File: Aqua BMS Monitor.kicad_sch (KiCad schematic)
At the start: 92 parts, among them J1 Conn_01x05_Pin, J2 Conn_01x04, J3 Conn_01x02_Pin, J4 Conn_01x04, J5 Conn_01x04, Q1 NPN, Q2 NMOS, Q3 NMOS, Q4 PMOS, U1 BQ76952PFBR

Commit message: Initial setup and some organization
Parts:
- added C00, C1-0, C2-1, C3-2, C4-3: 220nF, symbol Device:C
- added Cellin1: 1 low 5 high, symbol Connector:Conn_01x05_Pin
- added MainBattIn: Main lines, symbol Connector:Conn_01x02_Pin
- added RC0, RC1, RC2, RC3, RC4: 20, symbol Device:R
- added TP12: TestPoint, symbol Connector:TestPoint
- Cellin: renamed from J1; value Conn_01x05_Pin -> 1 low 5 high
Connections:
- net 16P: no longer Cellin.5 (Pin_5), R1.1
- net VSS: now also C00.2, C1-0.2, MainBattIn.2 (Pin_2)
- net Cell3: now reaches U1.1 (VC15), U1.10 (VC6), U1.11 (VC5), U1.12 (VC4), U1.2 (VC14), U1.3 (VC13), U1.4 (VC12), U1.5 (VC11), U1.6 (VC10), U1.7 (VC9), U1.8 (VC8), U1.9 (VC7)
- net Cell3: now also U1.13 (VC3), C3-2.2, C4-3.1, RC3.2; no longer R1.2, U1.48 (VC16)
- net at C21.2, R2.2: no longer U1.13 (VC3)
- net at C1.2, C21.1, R3.2: no longer U1.14 (VC2)
- net at C1.1, C3.1, R4.2: no longer U1.15 (VC1)
- new net: Cellin1.4 (Pin_4), RC3.1
- new net: C4.1, Cellin.1 (Pin_1), TP5.1
- new net: Cellin1.2 (Pin_2), RC1.1
- new net: R8.2, R9.2, TP6.1
- new net: Cellin1.1 (Pin_1), RC0.1
- new net: Cellin1.3 (Pin_3), RC2.1
- new net: Cellin1.5 (Pin_5), RC4.1
- new net BAT+: MainBattIn.1 (Pin_1)
- new net Cell0: C00.1, RC0.2, TP12.1, U1.16 (VC0)
- new net Cell1: C1-0.1, C2-1.1, RC1.2, U1.15 (VC1)
- new net Cell2: C2-1.2, C3-2.1, RC2.2, U1.14 (VC2)
- new net Cell4: C4-3.2, RC4.2, U1.48 (VC16)
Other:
- note added: "Battery in"
- note added: "Cells"
- note added: "Grounding will be something to look at, cells are not necessarly attached to ground normally"
- note added: "Needs tie to ground, I think this right..."
- moved on the sheet: C1, C10, C15, C16, C2, C21, C28, C29, C3, C30, C31, C4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

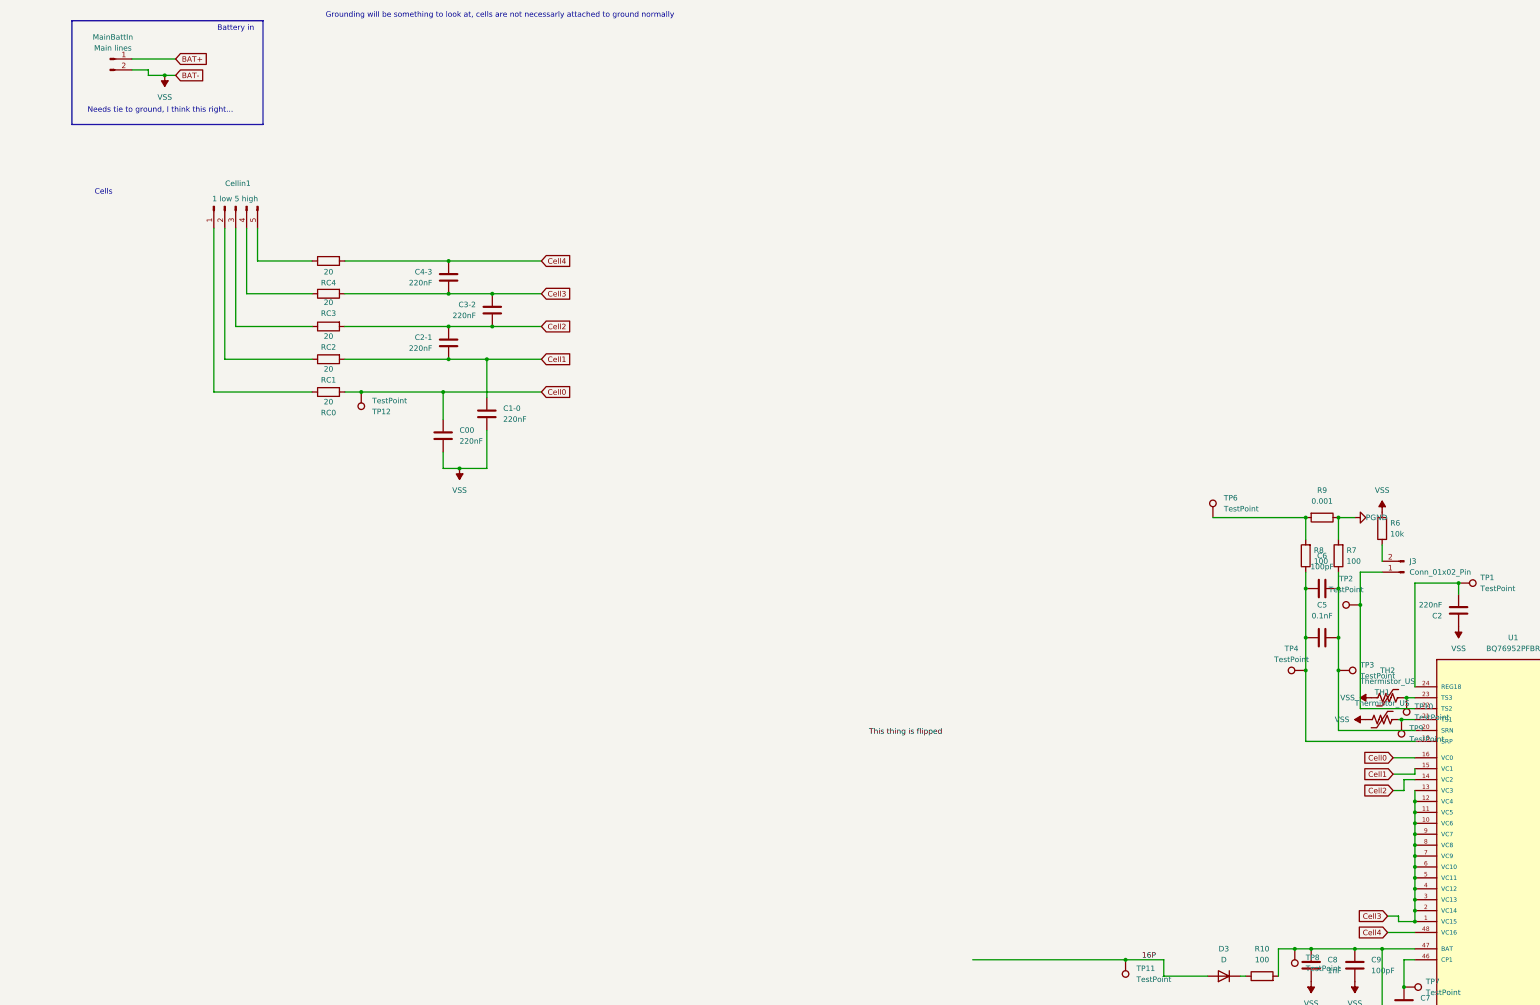
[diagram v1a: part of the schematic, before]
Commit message: Updates
Cell monitor and shunt resistor complete
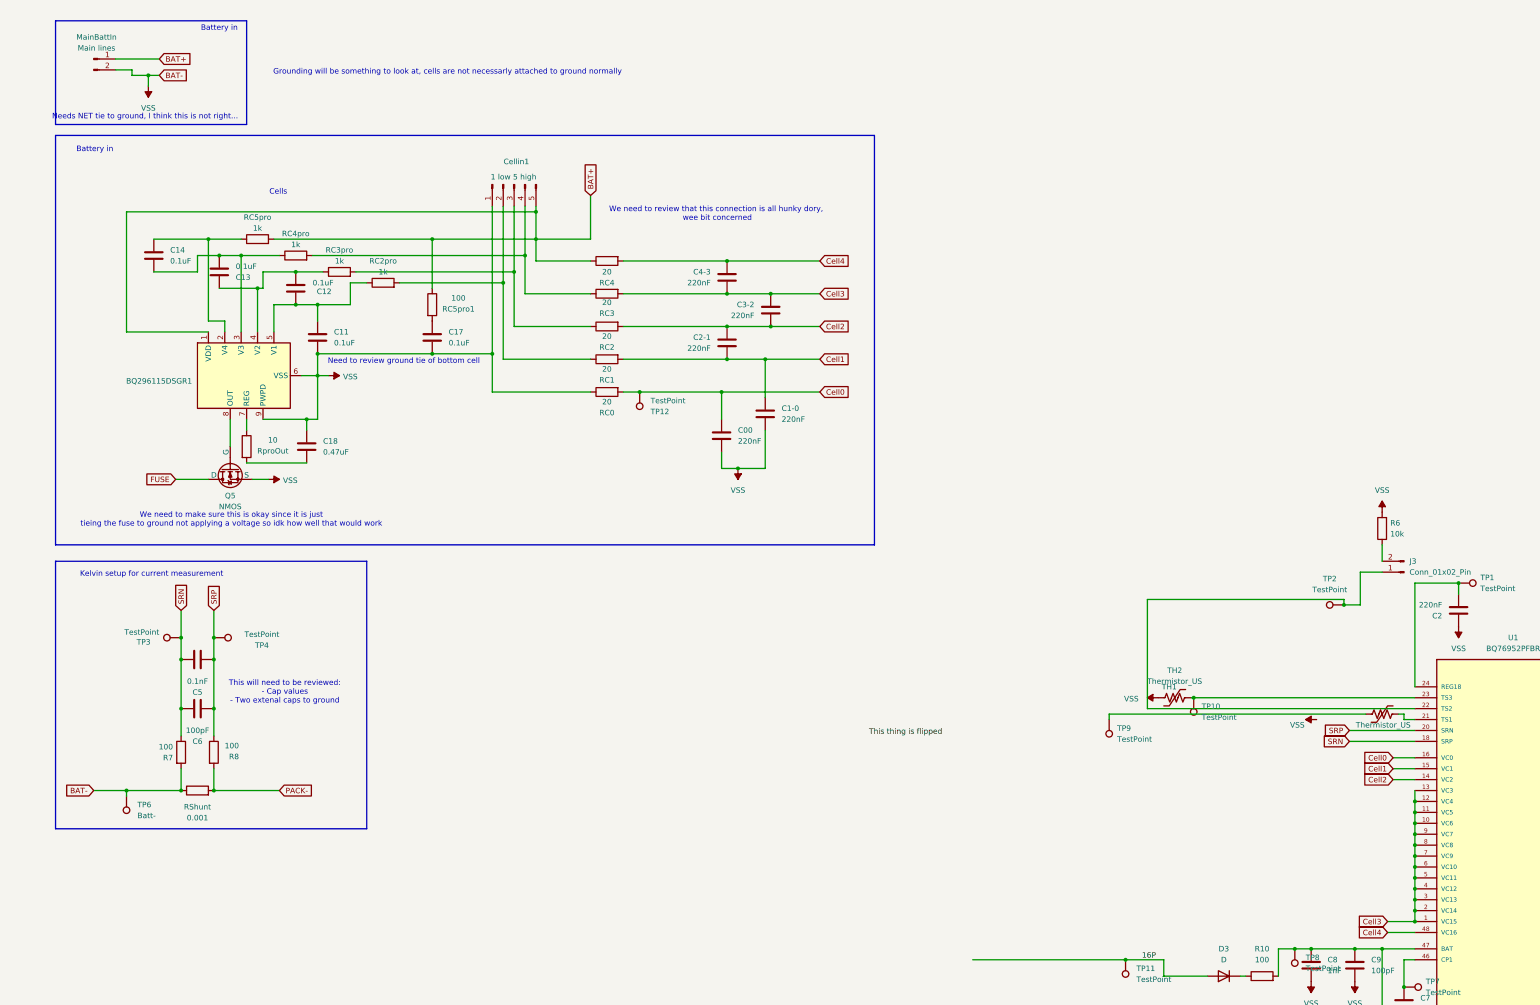
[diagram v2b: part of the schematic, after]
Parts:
- added BQ296115DSGR1: ~, symbol New_Library:BQ296115DSGR
- added C11, C12, C13, C14, C17: 0.1uF, symbol Device:C
- added C18: 0.47uF, symbol Device:C
- added Q5: NMOS, symbol Simulation_SPICE:NMOS
- added RC2pro, RC3pro, RC4pro, RC5pro: 1k, symbol Device:R
- added RC5pro1: 100, symbol Device:R
- added RproOut: 10, symbol Device:R
- TP6: value TestPoint -> Batt-
- renumbered R9 to RShunt
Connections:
- net BAT+: now also Cellin1.5 (Pin_5), RC4.1, BQ296115DSGR1.1 (VDD), RC5pro.2, RC5pro1.1
- net PGND: no longer R7.2, RShunt.1
- net VSS: now also Cellin1.1 (Pin_1), R7.2, RC0.1, RShunt.1, TP6.1, BQ296115DSGR1.6 (VSS), BQ296115DSGR1.9 (PWPD), C11.1, C17.2, C18.1, Q5.3 (S); no longer TH1.1
- net at Cellin1.4 (Pin_4), RC3.1: now also RC4pro.2
- net SRP: now reaches C5.2, C6.2, R8.1, TP4.1
- net SRP: now also U1.20 (SRN); no longer U1.18 (SRP)
- net SRN: now reaches C5.1, C6.1, R7.1, TP3.1
- net SRN: now also U1.18 (SRP); no longer U1.20 (SRN)
- net at TH1.2, U1.21 (TS1): no longer TP9.1
- net at Cellin1.2 (Pin_2), RC1.1: now also RC2pro.2
- net PACK-: now reaches R8.2, RShunt.2
- net PACK-: no longer TP6.1
- net at Cellin1.3 (Pin_3), RC2.1: now also RC3pro.2
- new net: BQ296115DSGR1.2 (V4), C14.1, RC5pro.1
- new net: BQ296115DSGR1.3 (V3), C13.2, C14.2, RC4pro.1
- new net: TH1.1, TP9.1
- new net: C17.1, RC5pro1.2
- new net: BQ296115DSGR1.5 (V1), C11.2, C12.1, RC2pro.1
- new net: BQ296115DSGR1.4 (V2), C12.2, C13.1, RC3pro.1
- new net: BQ296115DSGR1.8 (OUT), Q5.2 (G)
- new net: BQ296115DSGR1.7 (REG), RproOut.1
- new net: C18.2, RproOut.2
- new net FUSE: Q5.1 (D)
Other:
- note added: "Kelvin setup for current measurement"
- note added: "Need to review ground tie of bottom cell"
- note added: "Needs NET tie to ground, I think this is not right..."
- note added: "This will need to be reviewed: - Cap values - Two extenal caps to ground"
- note added: "We need to make sure this is okay since it is just tieing the fuse to ground not applying a voltage so idk how well that would work"
- note added: "We need to review that this connection is all hunky dory, wee bit concerned"
- note removed: "Needs tie to ground, I think this right..."
- moved on the sheet: C00, C1-0, C2-1, C3-2, C4-3, C5, C6, Cellin1, MainBattIn, R7, R8, RC0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

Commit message: Updates
Thermosister and BAT/CP1 circuit updated
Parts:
- removed C21: 220nF, symbol Device:C
- removed C7: 0.47nF, symbol Device:C
- removed C8: 1nF, symbol Device:C
- removed C9: 100pF, symbol Device:C
- removed Cellin: 1 low 5 high, symbol Connector:Conn_01x05_Pin
- removed D3: D, symbol Device:D
- removed J3: Conn_01x02_Pin, symbol Connector:Conn_01x02_Pin
- removed R10: 100, symbol Device:R
- removed R2, R3, R4: 20, symbol Device:R
- removed R6: 10k, symbol Device:R
- removed TH1, TH2: Thermistor_US, symbol Device:Thermistor_US
- removed TP10, TP11, TP7, TP8: TestPoint, symbol Connector:TestPoint
- added D3: 100V, symbol Device:D_Schottky
- added J1: Conn_01x02_Pin, symbol Connector:Conn_01x02_Pin
- added R9: 10k, symbol Device:R
- added TH3, TH4: Thermistor_US, symbol Device:Thermistor_US
- added TP13, TP14, TP15: TestPoint, symbol Connector:TestPoint
- C1: value 220nF -> 1nF
- C3: value 220nF -> 100pF
- C4: value 220nF -> 0.47nF
- R1: value 20 -> 100
- TP2: value TestPoint -> BAT+
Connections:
- net BAT+: now also TP2.1, D3.2 (A)
- net VSS: now also C1.2, R9.2, TH3.2, TH4.2; no longer C4.2
- net BAT: now reaches U1.47 (BAT)
- net BAT: now also C1.1, C3.1, C4.1, R1.2, TP5.1
- net TS1: now reaches U1.21 (TS1)
- net TS1: now also TH3.1, TP14.1
- net TS2: now reaches U1.22 (TS2)
- net TS2: now also J1.1 (Pin_1), TP15.1; no longer TP2.1
- net TS3: now reaches U1.23 (TS3)
- net TS3: now also TH4.1, TP13.1
- net CP1: now reaches U1.46 (CP1)
- net CP1: now also C4.2, TP9.1
- net at R1.1: now also D3.1 (K)
- new net: J1.2 (Pin_2), R9.1
- no-connect marks 0 -> 1
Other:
- note added: "- values will likely need to be better tailored to our application - CP will likely be used, but depends on main line circuit"
- note added: "Battery and Charge pump circuit"
- note added: "TS1, TS2, TS3 circuit"
- note added: "This guy is meant for wake ups this could likely become another themistor While it is two extenrnal connection pins we need to figure this out If this is the only way to wake the cell up we'll need this because getting slept would suck"
- moved on the sheet: C2, D1, D2, GD1, GD2, J2, R22, TP1

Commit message: Main circuits done
All circuits I (kinda) understand are organised
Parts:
- removed C16: 22nF, symbol Device:C
- removed C28, C29: 0.1uF, symbol Device:C
- removed D1, D2: D_TVS, symbol Device:D_TVS
- removed D4: D_Zener, symbol Device:D_Zener
- removed D5, D6, D7: 16V, symbol Device:D_Zener
- removed D7: 100V, symbol Device:D_Zener
- removed D8: 100V, symbol Device:D_Schottky
- removed GD1, GD2: GDT_2Pin, symbol Device:GDT_2Pin
- removed J2: Conn_01x04, symbol Connector_Generic:Conn_01x04
- removed Q1: NPN, symbol Simulation_SPICE:NPN
- removed Q2, Q3: NMOS, symbol Simulation_SPICE:NMOS
- removed Q4: PMOS, symbol Simulation_SPICE:PMOS
- removed R22: R 1.0k, symbol Device:R
- removed R31: R 10M, symbol BQ76952PFBR:R
- removed R32, R33: 10M, symbol BQ76952PFBR:R
- removed R34: 0, symbol BQ76952PFBR:R
- removed R35: 10k, symbol BQ76952PFBR:R
- removed R37, R39, R41, R42, R43, R44, R45: R 5.1k, symbol BQ76952PFBR:R
- removed R40: R 7.5k, symbol BQ76952PFBR:R
- removed TP16, TP17, TP19, TP22, TP23: TestPoint, symbol Connector:TestPoint
- added C7: 0.1uF, symbol Device:C
- added C8: 1uF, symbol Device:C
- added C9: 22nF, symbol Device:C
- added D1: 100V, symbol Device:D_Zener
- added D10, D12, D9: 16V, symbol Device:D_Zener
- added D11: 100V, symbol Device:D_Schottky
- added D2: D_Zener, symbol Device:D_Zener
- added Q1, Q7: NMOS, symbol Simulation_SPICE:NMOS
- added Q6: NPN, symbol Simulation_SPICE:NPN
- added Q8: PMOS, symbol Simulation_SPICE:PMOS
- added R10, R13, R14, R3, R4, R6: R 5.1k, symbol BQ76952PFBR:R
- added R12: R 10M, symbol BQ76952PFBR:R
- added R16: R 7.5k, symbol BQ76952PFBR:R
- added R17: 0, symbol BQ76952PFBR:R
- added R18, R19: 10M, symbol BQ76952PFBR:R
- added R2: 300, symbol BQ76952PFBR:R
- added R21: 10k, symbol BQ76952PFBR:R
- added TP10, TP11, TP18, TP7, TP8: TestPoint, symbol Connector:TestPoint
- C15: value 1uF -> 0.1uF
- R11: value 300 -> R 5.1k
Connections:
- net BAT+: now also C10.1, D9.2 (A), Q1.1 (D), R12.2
- net FUSE: now also U1.38 (FUSE)
- net PGND: now also D11.2 (A)
- net REG1: now also C8.2; no longer C15.2
- net VSS: now also C7.2, C8.1, C9.2; no longer C10.2, C15.1
- net CHG: now reaches U1.45 (CHG)
- net CHG: now also R11.1, TP10.1
- net at R11.2: now also D9.1 (K), Q1.2 (G), R12.1, TP18.1
- net REGIN: now reaches U1.36 (REGIN)
- net REGIN: now also C9.1, Q6.3 (E)
- net BREG: now reaches U1.37 (BREG)
- net BREG: now also Q6.2 (B)
- net LD: now reaches U1.41 (LD)
- net LD: now also R4.1, TP8.1
- net PACK: now reaches U1.42 (PACK)
- net PACK: now also R3.1, TP7.1; no longer TP21.1
- net DSG: now reaches U1.43 (DSG)
- net DSG: now also D2.1 (K), R14.1, TP11.1
- net PACK+: now reaches C30.1, E3.3, J5.1 (Pin_1), J5.2 (Pin_2)
- net PACK+: now also C15.2, TP21.1, D10.2 (A), D12.2 (A), Q7.3 (S), Q8.1 (D), R10.2, R18.2, R19.2, R6.2
- new net: D11.1 (K), R21.1
- new net: D12.1 (K), Q8.2 (G), R19.1, R21.2
- new net: R13.1, R14.2
- new net: D10.1 (K), Q8.3 (S), R13.2, R16.2, R17.1, R18.1
- new net: R10.1, R4.2
- new net: R3.2, R6.1
- new net: C10.2, C15.1
- new net: C7.1, Q6.1 (C), R2.1
- new net: Q7.2 (G), R17.2
- new net: D1.1 (K), R2.2
- new net: D2.2 (A), R16.1
- new net CD: D1.2 (A), Q1.3 (S), Q7.1 (D)
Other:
- note added: "Charge/Discharge circuit V1"
- note added: "I think these are not always tied to ground"
- note added: "Likely something we want in the big charge/discharge circuit"
- note added: "May be connect to something, may not!"
- note added: "May need to change resistor value and arrangement"
- note added: "May need to meddle with values otherwise fine"
- note added: "Pack and LD setup"
- note added: "Reg circuit"
- note added: "This will likely be changed but idk for now"
- note added: "Whoops I accidently disconnected this"
- note added: "You need to figure out what net this is"
- moved on the sheet: R15, TP20

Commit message: Commits before fork
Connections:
- net BAT+: now also Q1.3 (S); no longer Q1.1 (D)
- net CD: now also Q1.1 (D); no longer Q1.3 (S)
- net VSS: no longer U1.29 (CFETOFF), U1.30 (DFETOFF)
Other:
- note added: "I think these are not always tied to ground, we may have a use case"
- note added: "connection protection"
- note removed: "I think these are not always tied to ground"
- moved on the sheet: C2, D5, D6, GD3, GD4, J4, Q1, R15, R20, R23, R24, R5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

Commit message: Big Updates
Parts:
- removed J1: Conn_01x02_Pin, symbol Connector:Conn_01x02_Pin
- added C16: 1uF, symbol Device:C
- added C19, C20, C21, C22: 0.1uF, symbol Device:C
- added D4: 100V, symbol Device:D_Schottky
- added D7: 100V, symbol Device:D_Zener
- added MainBattIn1: Main lines, symbol Connector:Conn_01x02_Pin
- added Q2, Q3: PMOS, symbol Simulation_SPICE:PMOS
- added R22: 10M, symbol Device:R
- added R25, R30: R 10M, symbol BQ76952PFBR:R
- added R26, R28: 1k, symbol BQ76952PFBR:R
- added R27, R29: 5.1k, symbol BQ76952PFBR:R
- added SW1: Button, symbol Switch:SW_DPST_x2
- added TP16, TP22: TestPoint, symbol Connector:TestPoint
- C4: value 0.47nF -> 0.47uF
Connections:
- net BAT+: now also C19.1, C21.1, Q3.3 (S), R26.1, R30.1
- net BREG: now also R22.2
- net TS2: now also SW1.1 (A)
- net VSS: now also C16.1, MainBattIn1.2 (Pin_2), R22.1
- net at D5.2 (A2), D6.2 (A2), GD4.3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: no longer GD3.3, R24.2
- net at J4.3 (Pin_3), U1.26 (SCL), U1.44 (NC): now also GD3.3, R24.2
- net REG2: now reaches U1.34 (REG2)
- net REG2: now also C16.2
- net PDSG: now reaches U1.39 (PDSG)
- net PDSG: now also R29.1
- net PCHG: now reaches U1.40 (PCHG)
- net PCHG: now also R27.1
- net at D3.1 (K), R1.1: now also D4.1 (K)
- net at R9.1: now also SW1.2 (B)
- net at D1.1 (K), R2.2: now also D7.1 (K)
- net Cell0 renamed Cell1-
- net Cell1 renamed Cell1+/2-
- net Cell2 renamed Cell2+/3-
- net Cell3 renamed Cell3+/4-
- net Cell4 renamed Cell4+
- net REG1 renamed MCU
- new net: Q3.1 (D), R28.1
- new net: Q2.1 (D), R26.2
- new net: Q2.2 (G), R25.1, R27.2
- new net: Q3.2 (G), R29.2, R30.2
- new net: C21.2, C22.1
- new net: C19.2, C20.1
- new net CPACK+: C20.2, Q2.3 (S), R25.2, TP22.1
- new net DPACK+: C22.2, R28.2, TP16.1
- new net PWR+: D4.2 (A), D7.2 (A), MainBattIn1.1 (Pin_1)
- no-connect marks 1 -> 2
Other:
- note added: "- values will likely need to be better tailored to our application - CP is the power for CHG or DSG - There is an in depth discussion on how to select these in the application report"
- note added: "44 should also be NC -> not present on this"
- note added: "Can be split for heat disipation - Vid 440"
- note added: "DDSG SCHG used for comunicating the status of the fet"
- note added: "External 12V supply in"
- note added: "Gate resistors used to keep turn off and transients from being too high"
- note added: "Needs to be one that includes the power right off the bat These include clock stretching hence it needs a MCU that can handle that"
- note added: "Pre Dsg/CHG and general attachment"
- note added: "Pull down and zener diode used to keep steady difference. Review zener application"
- note added: "This can often be 2.2uF"
- note added: "This guy is meant for wake ups this could likely become another themistor While it is two extenrnal connection pins we need to figure this out (TRM manual) If this is the only way to wake the cell up we'll need this because getting slept would suck We can add more thermistors if we would like, and also include noise filtering w par C (470pF"
- note added: "This will need to be reviewed: - Cap values - Two extenal caps to ground - Shunt resistor value on CC and curr requirements"
- note added: "Vid 1uF"
- note added: "We can use these pins to turn Charge and discharge planes off CDFETOFF"
- note added: "We need to check in the connection configuration and how we include a protection, This is well documented on their sheets, but I do not want to hurt our batteries accidentally"
- note added: "currently no need for it, may need to check for turn on transients from the shut off or cap"
- note removed: "- values will likely need to be better tailored to our application - CP will likely be used, but depends on main line circuit"
- note removed: "This guy is meant for wake ups this could likely become another themistor While it is two extenrnal connection pins we need to figure this out If this is the only way to wake the cell up we'll need this because getting slept would suck"
- note removed: "This will need to be reviewed: - Cap values - Two extenal caps to ground"
- moved on the sheet: D1

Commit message: V1 Parellel paths
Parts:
- added C23, C24, C25, C26: 0.1uF, symbol Device:C
- added CPACK+: PACK-, symbol Connector:Conn_01x02_Pin
- added Q4, Q9: NMOS, symbol Simulation_SPICE:NMOS
- added R31: 51?, symbol BQ76952PFBR:R
- added R32: 1.0k, symbol BQ76952PFBR:R
- added R33: 10M, symbol BQ76952PFBR:R
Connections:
- net CD: now also C24.1, Q4.1 (D), Q9.1 (D), R33.1
- net PACK+: now also C23.2, C25.2, CPACK+.2 (Pin_2), Q4.3 (S), R32.1
- net PDSG: now also Q9.2 (G), R33.2
- net PGND: now also C26.1, CPACK+.1 (Pin_1)
- net at D10.1 (K), Q8.3 (S), R13.2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: now also R31.1
- new net: C23.1, C24.2
- new net: Q9.3 (S), R32.2
- new net: C25.1, C26.2
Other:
- note added: "(This fet has diode going other way Q4)"
- note added: "PCgate with Q3 fet and Cgate with Q2 fet doesnt exist cuz CD it different?"
- note added: "This CD part look nothing like the og schematic?"
- moved on the sheet: C10, C15, TP21
